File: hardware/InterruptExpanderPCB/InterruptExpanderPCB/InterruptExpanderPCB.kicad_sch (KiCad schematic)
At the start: 43 parts, among them J1 Conn_01x06_Pin, J2 Conn_01x08_Pin, J3 Conn_01x08_Pin, J4 Conn_01x01_Pin, U1 ATTINY85-20SU, U2 SN74HC251PWR, U3 SN74HC590ADT, U4 SN74HCT138PWRE4, U5 74AHC1G08

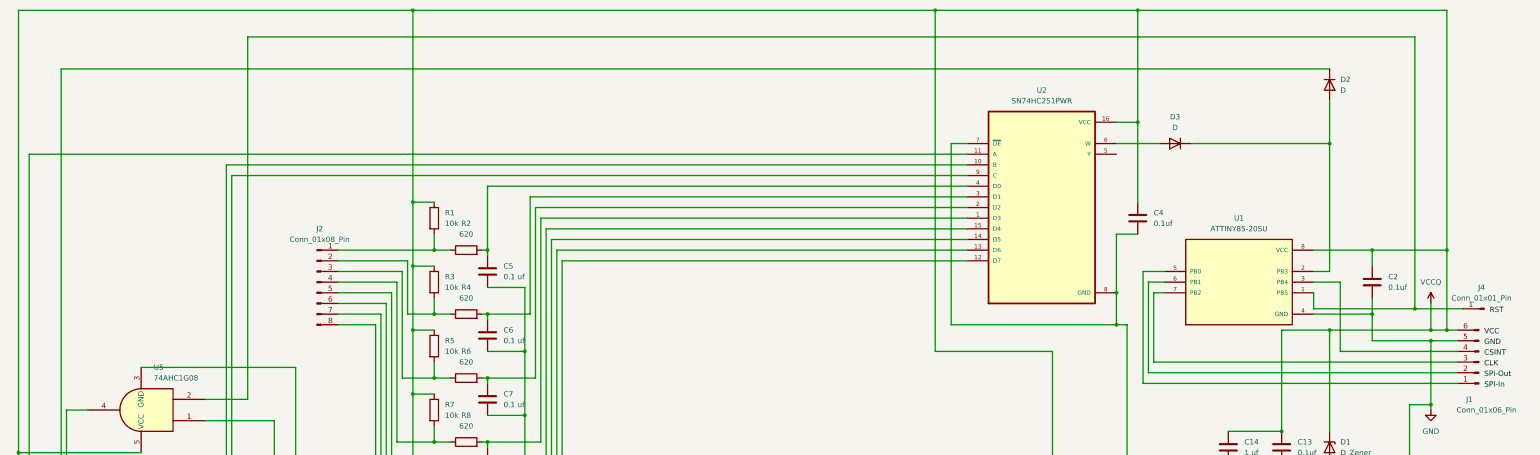
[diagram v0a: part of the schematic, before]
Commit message: Fixed an issue identified with hardware for shared clock read and write functions. Fixed issue with SPI loop on firmware
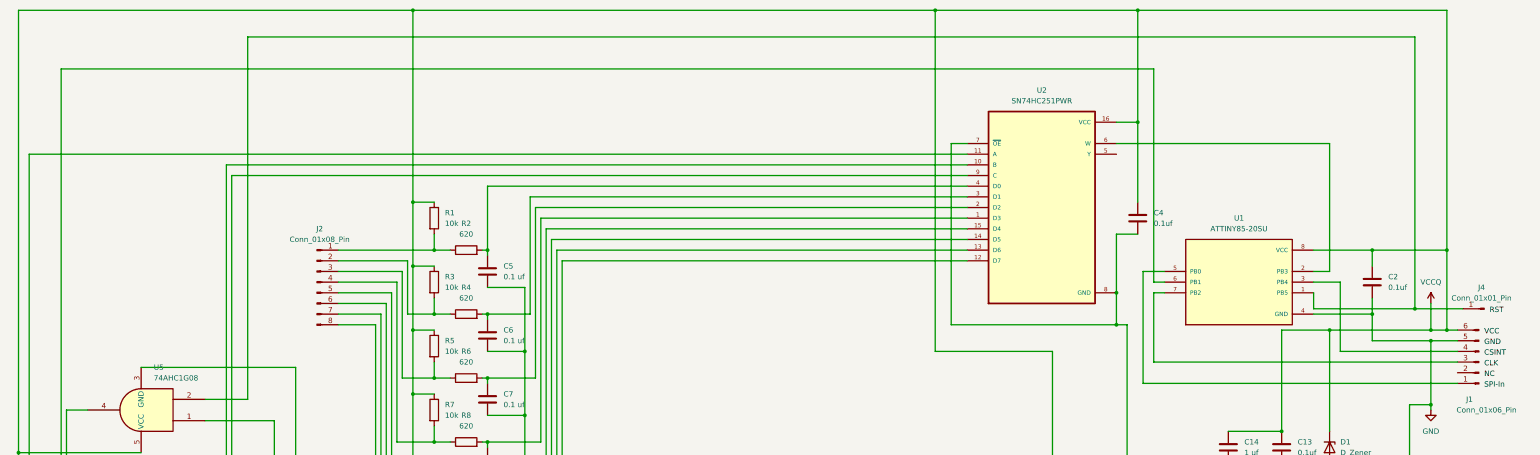
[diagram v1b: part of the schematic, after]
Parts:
- removed D2, D3: D, InterrupterLibrary:RF01128, symbol Device:D
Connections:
- net at R17.1, U3.11 (CCLK), U3.13 (RCLK): now also U1.6 (PB1)
- net at J1.2 (Pin_2): no longer U1.6 (PB1)
- net at U2.6 (W): now also U1.2 (PB3)
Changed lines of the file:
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@@
 	)
 	(junction
-		(at 327.66 53.34)
-		(diameter 0)
-		(color 0 0 0 0)
-	)
-	(junction
 		(at 127 158.75)
 		(diameter 0)
@@
 	(wire
 		(pts
-			(xy 284.48 86.36) (xy 284.48 107.95)
-		)
-		(stroke
-			(width 0)
-			(type default)
-		)
-	)
-	(wire
-		(pts
 			(xy 114.3 147.32) (xy 109.22 147.32)
 		)
@@
 	(wire
 		(pts
-			(xy 288.29 86.36) (xy 284.48 86.36)
-		)
-		(stroke
-			(width 0)
-			(type default)
-		)
-	)
-	(wire
-		(pts
 			(xy 91.44 91.44) (xy 102.87 91.44)
 		)
@@
 	(wire
 		(pts
+			(xy 288.29 86.36) (xy 285.75 86.36)
+		)
+		(stroke
+			(width 0)
+			(type default)
+		)
+	)
+	(wire
+		(pts
 			(xy 19.05 176.53) (xy 25.4 176.53)
 		)
@@
 	(wire
 		(pts
+			(xy 285.75 35.56) (xy 285.75 86.36)
+		)
+		(stroke
+			(width 0)
+			(type default)
+		)
+	)
+	(wire
+		(pts
 			(xy 316.23 132.08) (xy 327.66 132.08)
 		)
@@
 	(wire
 		(pts
-			(xy 327.66 43.18) (xy 327.66 53.34)
-		)
-		(stroke
-			(width 0)
-			(type default)
-		)
-	)
-	(wire
-		(pts
 			(xy 127 78.74) (xy 125.73 78.74)
 		)
@@
 	(wire
 		(pts
-			(xy 294.64 53.34) (xy 327.66 53.34)
-		)
-		(stroke
-			(width 0)
-			(type default)
-		)
-	)
-	(wire
-		(pts
 			(xy 25.4 157.48) (xy 29.21 157.48)
 		)
@@
 	(wire
 		(pts
-			(xy 284.48 107.95) (xy 358.14 107.95)
-		)
-		(stroke
-			(width 0)
-			(type default)
-		)
-	)
-	(wire
-		(pts
 			(xy 337.82 78.74) (xy 355.6 78.74)
 		)
@@
 	(wire
 		(pts
-			(xy 276.86 53.34) (xy 287.02 53.34)
+			(xy 276.86 53.34) (xy 327.66 53.34)
 		)
 		(stroke
@@
 	(wire
 		(pts
-			(xy 25.4 35.56) (xy 327.66 35.56)
+			(xy 25.4 35.56) (xy 285.75 35.56)
 		)
 		(stroke
@@
 		)
 	)
-	(label "SPI-Out"
+	(label "NC"
 		(at 364.49 109.22 0)
 		(fields_autoplaced yes)
@@
 	)
 	(symbol
-		(lib_id "Device:D")
-		(at 290.83 53.34 180)
-		(unit 1)
-		(exclude_from_sim no)
-		(in_bom yes)
-		(on_board yes)
-		(dnp no)
-		(fields_autoplaced yes)
-		(property "Reference" "D3"
-			(at 290.83 46.99 0)
-			(effects
-				(font
-					(size 1.27 1.27)
-				)
-			)
-		)
-		(property "Value" "D"
-			(at 290.83 49.53 0)
-			(effects
-				(font
-					(size 1.27 1.27)
-				)
-			)
-		)
-		(property "Footprint" "InterrupterLibrary:RF01128"
-			(at 290.83 53.34 0)
-			(effects
-				(font
-					(size 1.27 1.27)
-				)
-				(hide yes)
-			)
-		)
-		(property "Datasheet" "~"
-			(at 290.83 53.34 0)
-			(effects
-				(font
-					(size 1.27 1.27)
-				)
-				(hide yes)
-			)
-		)
-		(property "Description" "Diode"
-			(at 290.83 53.34 0)
-			(effects
-				(font
-					(size 1.27 1.27)
-				)
-				(hide yes)
-			)
-		)
-		(property "Sim.Device" "D"
-			(at 290.83 53.34 0)
-			(effects
-				(font
-					(size 1.27 1.27)
-				)
-				(hide yes)
-			)
-		)
-		(property "Sim.Pins" "1=K 2=A"
-			(at 290.83 53.34 0)
-			(effects
-				(font
-					(size 1.27 1.27)
-				)
-				(hide yes)
-			)
-		)
-		(pin "1"
-		)
-		(pin "2"
-		)
-		(instances
-			(project "InterruptExpanderPCB"
-				(path "/e63e39d7-6ac0-4ffd-8aa3-1841a4541b55"
-					(reference "D3")
-					(unit 1)
-				)
-			)
-		)
-	)
-	(symbol
 		(lib_id "Device:C")
 		(at 127 163.83 0)
@@
 					(unit 1)
 				)
-			)
-		)
-	)
-	(symbol
-		(lib_id "Device:D")
-		(at 327.66 39.37 270)
-		(unit 1)
-		(exclude_from_sim no)
-		(in_bom yes)
-		(on_board yes)
-		(dnp no)
-		(fields_autoplaced yes)
-		(property "Reference" "D2"
-			(at 330.2 38.0999 90)
-			(effects
-				(font
-					(size 1.27 1.27)
-				)
-				(justify left)
-			)
-		)
-		(property "Value" "D"
-			(at 330.2 40.6399 90)
-			(effects
-				(font
-					(size 1.27 1.27)
-				)
-				(justify left)
-			)
-		)
-		(property "Footprint" "InterrupterLibrary:RF01128"
-			(at 327.66 39.37 0)
-			(effects
-				(font
-					(size 1.27 1.27)
-				)
-				(hide yes)
-			)
-		)
-		(property "Datasheet" "~"
-			(at 327.66 39.37 0)
-			(effects
-				(font
-					(size 1.27 1.27)
-				)
-				(hide yes)
-			)
-		)
-		(property "Description" "Diode"
-			(at 327.66 39.37 0)
-			(effects
-				(font
-					(size 1.27 1.27)
-				)
-				(hide yes)
-			)
-		)
-		(property "Sim.Device" "D"
-			(at 327.66 39.37 0)
-			(effects
-				(font
-					(size 1.27 1.27)
-				)
-				(hide yes)
-			)
-		)
-		(property "Sim.Pins" "1=K 2=A"
-			(at 327.66 39.37 0)
-			(effects
-				(font
-					(size 1.27 1.27)
-				)
-				(hide yes)
-			)
-		)
-		(pin "1"
-		)
-		(pin "2"
-		)
-		(instances
-			(project ""
-				(path "/e63e39d7-6ac0-4ffd-8aa3-1841a4541b55"
-					(reference "D2")
-					(unit 1)
-				)
